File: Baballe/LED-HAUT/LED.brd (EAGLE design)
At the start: 30 x 32 mm, 15 parts, among them Q1 200mA/50V, Q2 200mA/50V, Q3 200mA/50V

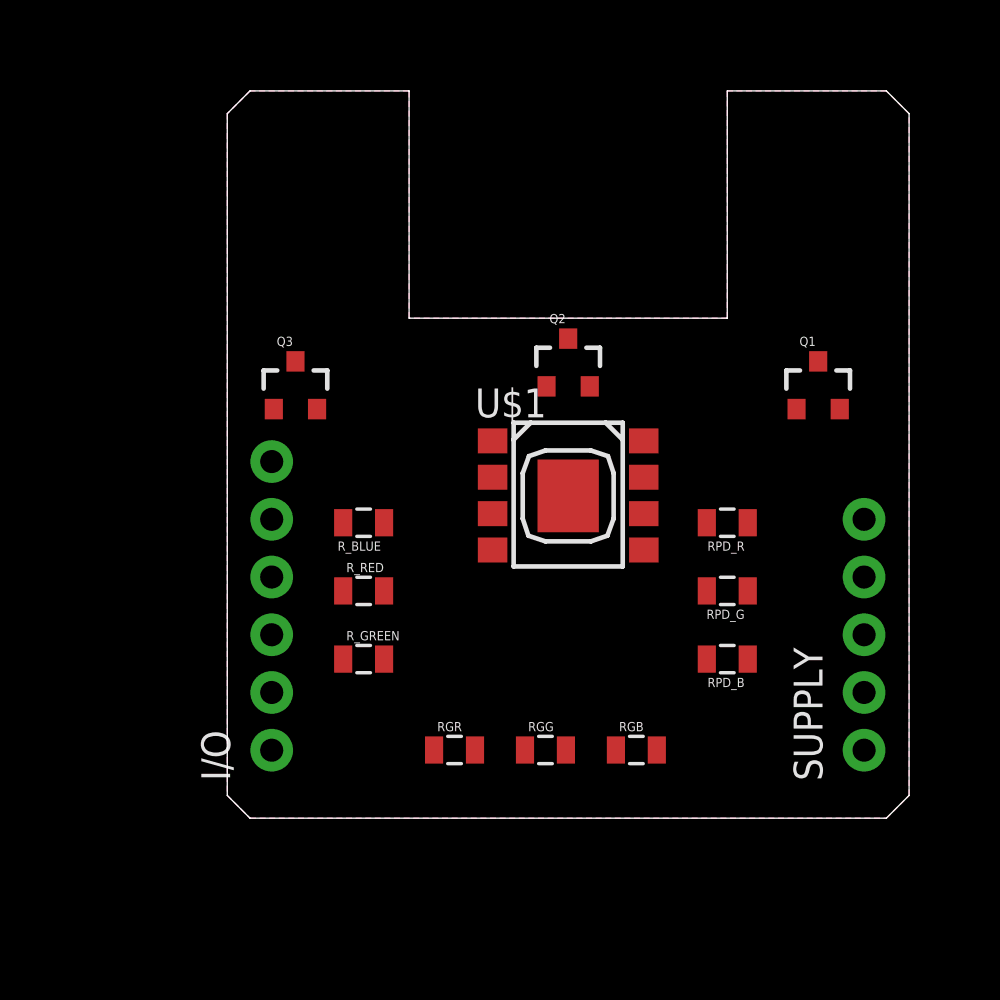
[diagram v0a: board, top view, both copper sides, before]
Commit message: Modification sur les modules led et alimentation
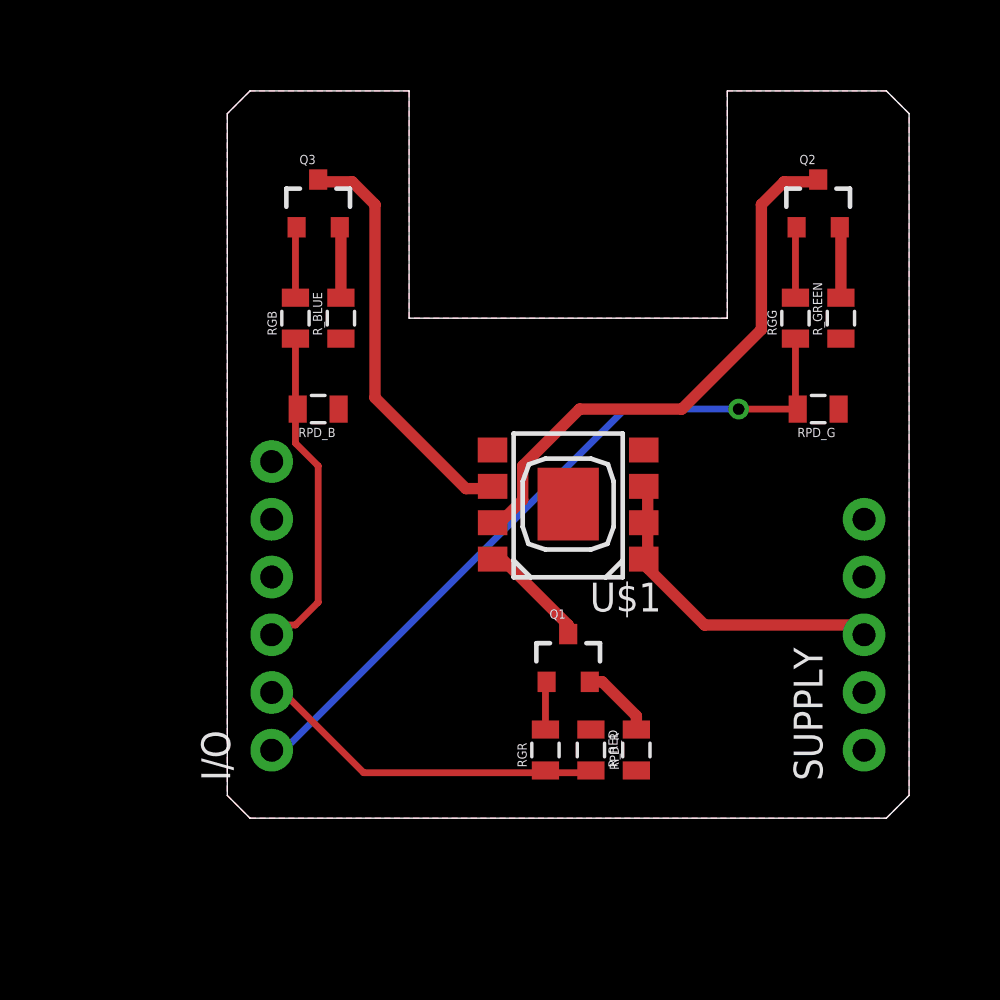
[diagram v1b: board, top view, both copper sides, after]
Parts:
- U$1: value LED -> (none)
- moved R_GREEN 25.8 mm to (71.0, 22.0), turned to 90 degrees
- moved RGB 24.2 mm to (47.0, 22.0), turned to 90 degrees
- moved RGG 22.0 mm to (69.0, 22.0), turned to 90 degrees
- moved RPD_B 21.1 mm to (48.0, 18.0)
- moved Q1 16.3 mm to (59.0, 7.00)
- moved R_RED 13.9 mm to (62.0, 3.00), turned to 90 degrees
- moved Q2 13.0 mm to (70.0, 27.0)
- moved RPD_R 11.7 mm to (60.0, 3.00), turned to 270 degrees
- moved R_BLUE 9.06 mm to (49.0, 22.0), turned to 90 degrees
- moved RPD_G 8.94 mm to (70.0, 18.0)
- moved Q3 8.06 mm to (48.0, 27.0)
- moved RGR 4.00 mm to (58.0, 3.00), turned to 90 degrees
- moved U$1 2.00 mm to (59.0, 13.0), turned to 180 degrees
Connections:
- net N$7: now also U$1.5; no longer U$1.1
- net N$8: now also U$1.6; no longer U$1.3
- net N$9: now also U$1.7; no longer U$1.5
- net V_IN: now also U$1.1, U$1.3; no longer U$1.4, U$1.6
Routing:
- net O_GREEN: track 0.00 -> 33.1 mm, vias 0 -> 1
- net N$8: track 0.00 -> 24.7 mm
- net N$9: track 0.00 -> 18.4 mm
- net O_RED: track 0.00 -> 16.3 mm
- net V_IN: track 0.00 -> 15.0 mm
- net O_BLUE: track 0.00 -> 15.0 mm
- net N$7: track 0.00 -> 4.98 mm
- net N$3: track 0.00 -> 3.27 mm
- net N$6: track 0.00 -> 3.15 mm
- net N$4: track 0.00 -> 3.15 mm
- net N$2: track 0.00 -> 3.15 mm
- net N$1: track 0.00 -> 3.15 mm
- net N$5: track 0.00 -> 2.15 mm

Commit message: V2 de la Baballe
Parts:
- moved Q2 26.1 mm to (56.0, 5.00)
- moved RGG 25.2 mm to (55.0, 1.00)
- moved RPD_G 20.2 mm to (59.0, 1.00), turned to 270 degrees
- moved R_GREEN 19.7 mm to (63.0, 4.00), turned to 180 degrees
- moved Q3 18.7 mm to (50.0, 8.37), turned to 270 degrees
- moved R_BLUE 15.1 mm to (47.0, 7.00)
- moved RPD_R 11.0 mm to (49.0, 4.00), turned to 90 degrees
- moved RGB 9.22 mm to (49.0, 13.0), turned to 270 degrees
- moved RGR 6.40 mm to (63.0, 7.00), turned to 180 degrees
- moved R_RED 6.08 mm to (63.0, 9.00), turned to 180 degrees
- moved SUPPLY 4.02 mm to (68.0, 2.63)
- moved U$1 3.08 mm to (56.0, 13.7), turned to 270 degrees
- moved I/O 2.24 mm to (44.0, 1.99)
- moved RPD_B 1.41 mm to (49.0, 17.0), turned to 270 degrees
- moved Q1 1.00 mm to (59.0, 8.00), turned to 90 degrees
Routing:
- net N$8: track 24.7 -> 4.82 mm
- net O_GREEN: track 33.1 -> 15.9 mm, vias 1 -> 0
- net N$9: track 18.4 -> 5.51 mm
- net O_RED: track 16.3 -> 21.7 mm
- net V_IN: track 15.0 -> 18.1 mm
- net N$2: track 3.15 -> 5.15 mm
- net N$7: track 4.98 -> 3.04 mm
- net O_BLUE: track 15.0 -> 13.1 mm
- net N$3: track 3.27 -> 2.17 mm
- net N$4: track 3.15 -> 2.12 mm
- net N$1: track 3.15 -> 2.20 mm
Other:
- board size 30 x 32 mm -> 36.1 x 36.1 mm

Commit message: Baballe en attente de vérification finale
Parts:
- moved SUPPLY 0.60 mm to (68.0, 2.03)
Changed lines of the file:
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@@
 <setting verticaltext="up"/>
 </settings>
-<grid distance="0.1" unitdist="mm" unit="mm" style="lines" multiple="1" display="yes" altdistance="0.025" altunitdist="inch" altunit="inch"/>
+<grid distance="1" unitdist="mm" unit="mm" style="lines" multiple="1" display="yes" altdistance="0.025" altunitdist="inch" altunit="inch"/>
 <layers>
 <layer number="1" name="Top" color="4" fill="1" visible="yes" active="yes"/>
@@
 <attribute name="PROD_ID" value="CONN-08437" x="43.95533125" y="1.991" size="1.778" layer="27" rot="R90" display="off"/>
 </element>
-<element name="SUPPLY" library="SparkFun-Connectors" package="1X05_NO_SILK" value="SUPPLY" x="68.0188625" y="2.626" rot="R90"/>
+<element name="SUPPLY" library="SparkFun-Connectors" package="1X05_NO_SILK" value="SUPPLY" x="68.0188625" y="2.026" rot="R90"/>
 <element name="Q1" library="SparkFun-DiscreteSemi" package="SOT23-3" value="200mA/50V" x="59" y="8" rot="R90">
 <attribute name="PROD_ID" value="TRANS-00830" x="59" y="8" size="1.778" layer="27" rot="R90" display="off"/>
@@
 <contactref element="U$1" pad="3"/>
 <wire x1="59.1328" y1="16.8688" x2="57.3304" y2="16.8688" width="0.5" layer="1"/>
-<wire x1="67.9708" y1="7.7308" x2="59.1328" y2="16.8688" width="0.5" layer="1"/>
+<wire x1="61.9708" y1="13.7308" x2="59.1328" y2="16.8688" width="0.5" layer="1"/>
 <wire x1="57.3304" y1="16.8688" x2="57.6" y2="17.025" width="0.5" layer="1"/>
-<wire x1="67.9708" y1="7.7308" x2="68.0188625" y2="7.706" width="0.5" layer="1"/>
+<wire x1="61.9708" y1="13.7308" x2="68.0188625" y2="7.106" width="0.5" layer="1"/>
 <wire x1="56.1562" y1="16.8688" x2="54.5562" y2="16.8688" width="0.4064" layer="1"/>
 <wire x1="54.5562" y1="16.8688" x2="54.4" y2="17.025" width="0.4064" layer="1"/>
